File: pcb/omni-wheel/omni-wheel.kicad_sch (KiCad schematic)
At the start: 41 parts, among them IC1 AP63301WU-7, IC2 AP63301WU-7, J10 Conn_01x01_Pin, J11 Conn_01x01_Pin, J15 STLINK, J2 Motor2_output, J3 Motor4_output, J4 Motor3_output, J5 STLINK, J6 Motor1_output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

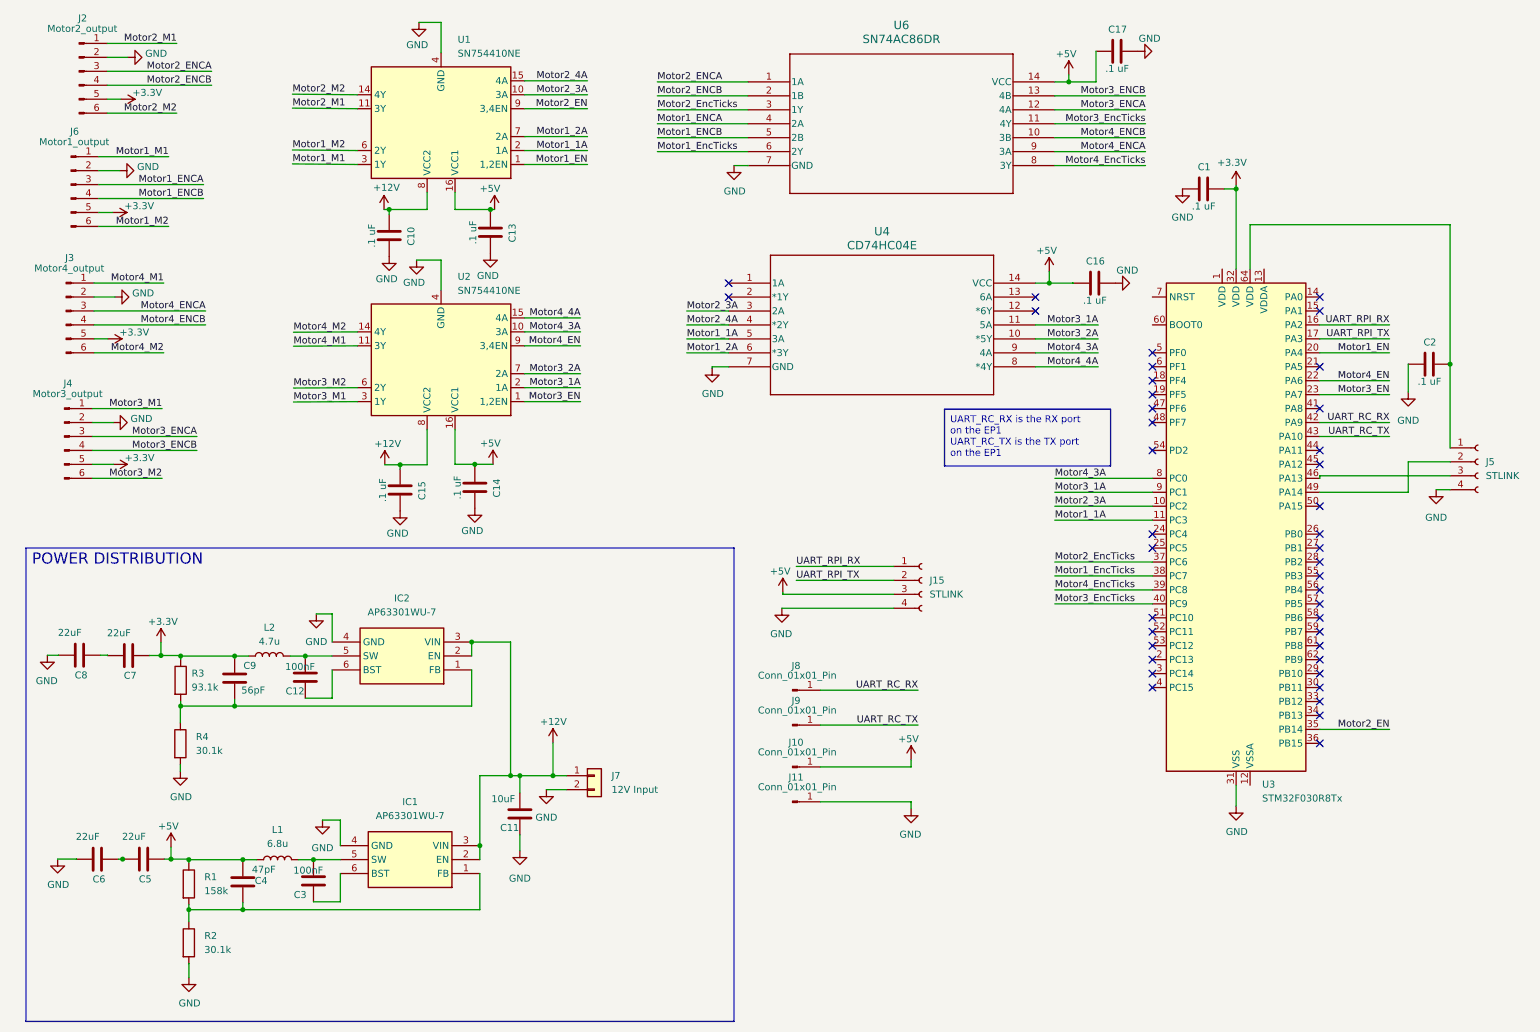
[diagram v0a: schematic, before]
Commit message: Added power test points to pcb, going to change xt size and add toggle switch next
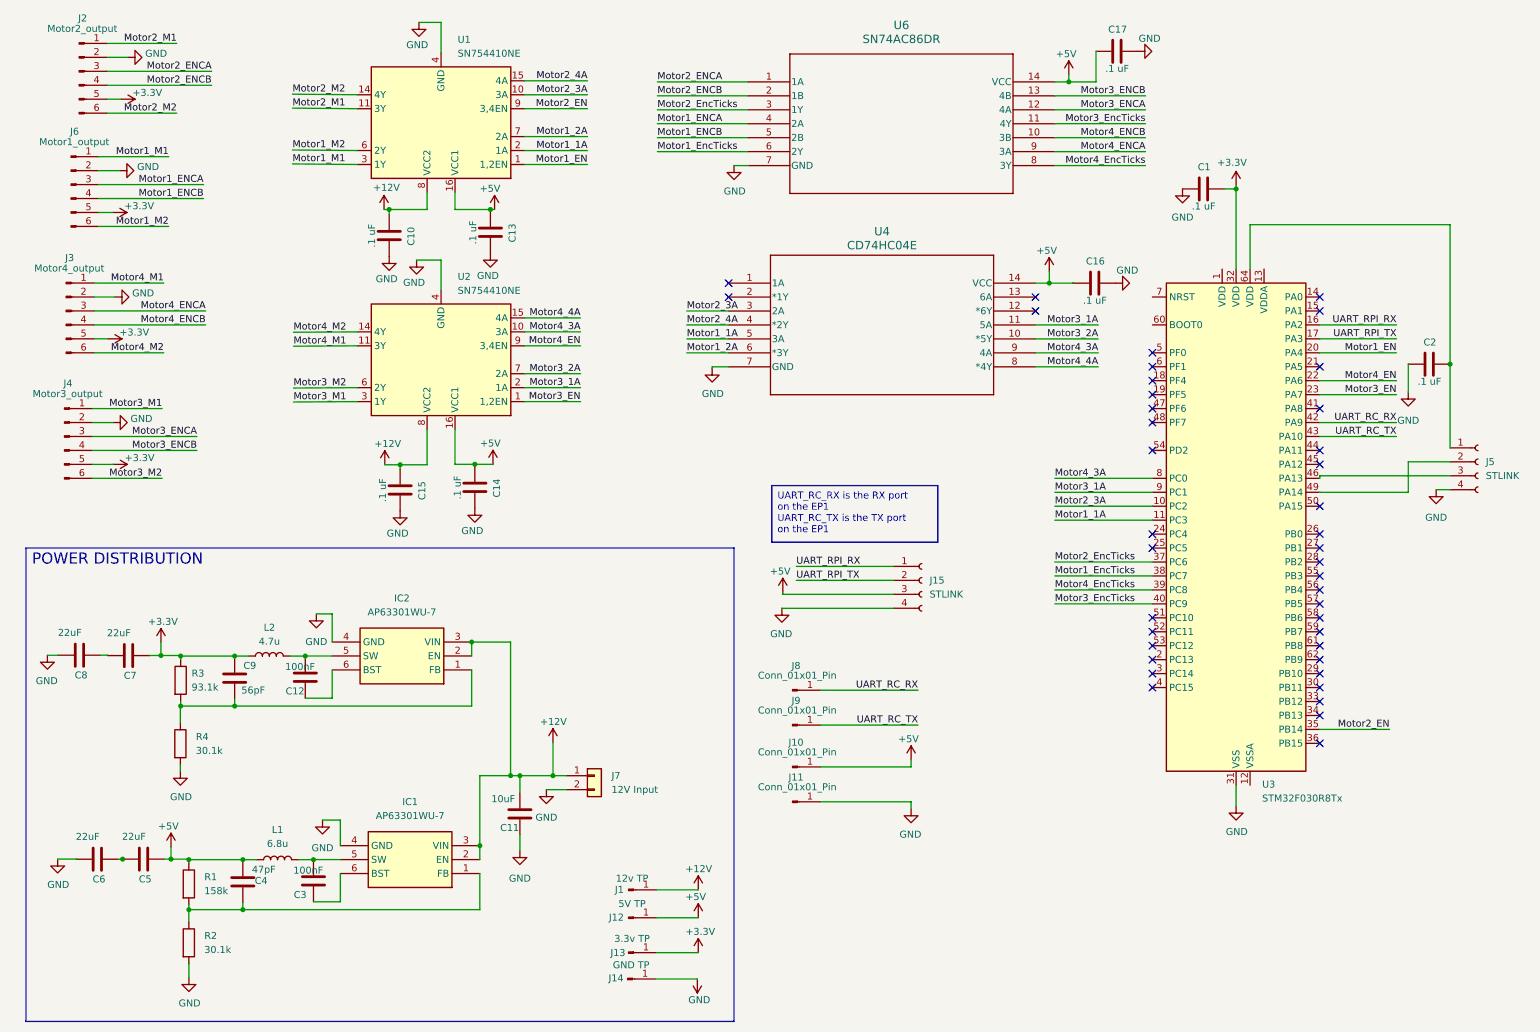
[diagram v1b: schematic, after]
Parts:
- added J1: 12v TP, TestPoint:TestPoint_THTPad_1.0x1.0mm_Drill0.5mm, symbol Connector:Conn_01x01_Pin
- added J12: 5V TP, TestPoint:TestPoint_THTPad_1.0x1.0mm_Drill0.5mm, symbol Connector:Conn_01x01_Pin
- added J13: 3.3v TP, TestPoint:TestPoint_THTPad_1.0x1.0mm_Drill0.5mm, symbol Connector:Conn_01x01_Pin
- added J14: GND TP, TestPoint:TestPoint_THTPad_1.0x1.0mm_Drill0.5mm, symbol Connector:Conn_01x01_Pin
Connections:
- net +12V: now also J1.1 (Pin_1)
- net +3.3V: now also J13.1 (Pin_1)
- net +5V: now also J12.1 (Pin_1)
- net GND: now also J14.1 (Pin_1)

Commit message: Added smaller xt connector and power switch
forgot to save schema
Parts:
- added SW1: SW_SPST, GF-123-0054:SW_GF-123-0054, symbol Switch:SW_SPST
- J7: footprint Connector_AMASS:AMASS_XT60PW-M_1x02_P7.20mm_Horizontal -> Connector_AMASS:AMASS_XT30PW-M_1x02_P2.50mm_Horizontal
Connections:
- net +12V: now also SW1.2 (B); no longer J7.1 (Pin_1)
- new net: J7.1 (Pin_1), SW1.1 (A)
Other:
- moved on the sheet: J7
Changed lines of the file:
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@@
 	)
 	(junction
-		(at 108.0081 153.2124)
-		(diameter 0)
-		(color 0 0 0 0)
-	)
-	(junction
 		(at 36.6238 131.3227)
 		(diameter 0)
@@
 	)
 	(junction
+		(at 107.9367 153.2124)
+		(diameter 0)
+		(color 0 0 0 0)
+	)
+	(junction
 		(at 40.2086 131.424)
 		(diameter 0)
@@
 	(wire
 		(pts
+			(xy 107.9367 153.0734) (xy 107.9367 153.2124)
+		)
+		(stroke
+			(width 0)
+			(type default)
+		)
+	)
+	(wire
+		(pts
 			(xy 261.62 81.28) (xy 247.65 81.28)
 		)
@@
 	(wire
 		(pts
-			(xy 106.8114 155.7524) (xy 106.8114 155.7504)
+			(xy 121.5026 155.4892) (xy 121.5026 157.4674)
 		)
 		(stroke
@@
 	(wire
 		(pts
+			(xy 109.5117 153.0734) (xy 107.9367 153.0734)
+		)
+		(stroke
+			(width 0)
+			(type default)
+		)
+	)
+	(wire
+		(pts
 			(xy 26.8028 27.4815) (xy 45.8528 27.4815)
 		)
@@
 	(wire
 		(pts
+			(xy 107.9367 153.2124) (xy 108.0081 153.2124)
+		)
+		(stroke
+			(width 0)
+			(type default)
+		)
+	)
+	(wire
+		(pts
 			(xy 78.1844 50.1004) (xy 85.09 50.1004)
 		)
@@
 	(wire
 		(pts
+			(xy 119.6717 153.0734) (xy 121.6382 153.0734)
+		)
+		(stroke
+			(width 0)
+			(type default)
+		)
+	)
+	(wire
+		(pts
 			(xy 69.2919 161.29) (xy 69.2919 165.9498)
 		)
@@
 	(wire
 		(pts
-			(xy 108.0081 153.2124) (xy 110.4721 153.2124)
-		)
-		(stroke
-			(width 0)
-			(type default)
-		)
-	)
-	(wire
-		(pts
 			(xy 54.0433 168.5038) (xy 51.5309 168.5038)
 		)
@@
 	(wire
 		(pts
-			(xy 110.4721 155.7524) (xy 106.8114 155.7524)
+			(xy 121.5026 155.4892) (xy 121.6382 155.4892)
 		)
 		(stroke
@@
 	(wire
 		(pts
+			(xy 121.6382 153.0734) (xy 121.6382 152.9492)
+		)
+		(stroke
+			(width 0)
+			(type default)
+		)
+	)
+	(wire
+		(pts
 			(xy 261.62 76.2) (xy 247.65 76.2)
 		)
@@
 	(wire
 		(pts
-			(xy 101.9818 153.2124) (xy 108.0081 153.2124)
+			(xy 101.9818 153.2124) (xy 107.9367 153.2124)
 		)
 		(stroke
@@
 	(symbol
 		(lib_id "Connector_Generic:Conn_01x02")
-		(at 115.5521 153.2124 0)
+		(at 126.7182 152.9492 0)
 		(unit 1)
 		(exclude_from_sim no)
@@
 		(fields_autoplaced yes)
 		(property "Reference" "J7"
-			(at 118.6738 153.2123 0)
+			(at 129.8399 152.9491 0)
 			(effects
 				(font
@@
 		)
 		(property "Value" "12V Input"
-			(at 118.6738 155.7523 0)
+			(at 129.8399 155.4891 0)
 			(effects
 				(font
@@
 			)
 		)
-		(property "Footprint" "Connector_AMASS:AMASS_XT60PW-M_1x02_P7.20mm_Horizontal"
-			(at 115.5521 153.2124 0)
+		(property "Footprint" "Connector_AMASS:AMASS_XT30PW-M_1x02_P2.50mm_Horizontal"
+			(at 126.7182 152.9492 0)
 			(effects
 				(font
@@
 		)
 		(property "Datasheet" "~"
-			(at 115.5521 153.2124 0)
+			(at 126.7182 152.9492 0)
 			(effects
 				(font
@@
 		)
 		(property "Description" "Generic connector, single row, 01x02, script generated (kicad-library-utils/schlib/autogen/connector/)"
-			(at 115.5521 153.2124 0)
+			(at 126.7182 152.9492 0)
 			(effects
 				(font
@@
 	)
 	(symbol
+		(lib_id "Switch:SW_SPST")
+		(at 114.5917 153.0734 180)
+		(unit 1)
+		(exclude_from_sim no)
+		(in_bom yes)
+		(on_board yes)
+		(dnp no)
+		(property "Reference" "SW1"
+			(at 114.411 150.7407 0)
+			(effects
+				(font
+					(size 1.27 1.27)
+				)
+			)
+		)
+		(property "Value" "SW_SPST"
+			(at 114.411 148.2007 0)
+			(effects
+				(font
+					(size 1.27 1.27)
+				)
+			)
+		)
+		(property "Footprint" "GF-123-0054:SW_GF-123-0054"
+			(at 114.5917 153.0734 0)
+			(effects
+				(font
+					(size 1.27 1.27)
+				)
+				(hide yes)
+			)
+		)
+		(property "Datasheet" "~"
+			(at 114.5917 153.0734 0)
+			(effects
+				(font
+					(size 1.27 1.27)
+				)
+				(hide yes)
+			)
+		)
+		(property "Description" "Single Pole Single Throw (SPST) switch"
+			(at 114.5917 153.0734 0)
+			(effects
+				(font
+					(size 1.27 1.27)
+				)
+				(hide yes)
+			)
+		)
+		(pin "2"
+		)
+		(pin "1"
+		)
+		(instances
+			(project ""
+				(path "/00bcea37-6431-4bf6-91e9-3738f9d2ffd8"
+					(reference "SW1")
+					(unit 1)
+				)
+			)
+		)
+	)
+	(symbol
 		(lib_id "power:+3.3V")
 		(at 134.3015 190.2313 180)
@@
 	(symbol
 		(lib_id "power:GND")
-		(at 106.8114 155.7504 0)
+		(at 121.5026 157.4674 0)
 		(unit 1)
 		(exclude_from_sim no)
@@
 		(fields_autoplaced yes)
 		(property "Reference" "#PWR019"
-			(at 106.8114 162.1004 0)
+			(at 121.5026 163.8174 0)
 			(effects
 				(font
@@
 		)
 		(property "Value" "GND"
-			(at 106.8114 160.8157 0)
+			(at 121.5026 162.5327 0)
 			(effects
 				(font
@@
 		)
 		(property "Footprint" ""
-			(at 106.8114 155.7504 0)
+			(at 121.5026 157.4674 0)
 			(effects
 				(font
@@
 		)
 		(property "Datasheet" ""
-			(at 106.8114 155.7504 0)
+			(at 121.5026 157.4674 0)
 			(effects
 				(font
@@
 		)
 		(property "Description" "Power symbol creates a global label with name \"GND\" , ground"
-			(at 106.8114 155.7504 0)
+			(at 121.5026 157.4674 0)
 			(effects
 				(font

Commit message: purchased this iteration of the board
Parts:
- SW1: digikey# (none) -> CWI333-ND; manf# (none) -> GF-123-0054
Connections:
- net GND: now also J7.1 (Pin_1); no longer J7.2 (Pin_2)
- net at SW1.1 (A): now also J7.2 (Pin_2); no longer J7.1 (Pin_1)
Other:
- moved on the sheet: J7
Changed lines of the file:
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@@
 	(wire
 		(pts
-			(xy 121.5026 155.4892) (xy 121.5026 157.4674)
-		)
-		(stroke
-			(width 0)
-			(type default)
-		)
-	)
-	(wire
-		(pts
 			(xy 93.2024 128.87) (xy 100.2871 128.87)
 		)
@@
 	(wire
 		(pts
+			(xy 124.3955 144.8826) (xy 121.6091 144.8826)
+		)
+		(stroke
+			(width 0)
+			(type default)
+		)
+	)
+	(wire
+		(pts
 			(xy 198.3856 63.5124) (xy 202.6638 63.5124)
 		)
@@
 	(wire
 		(pts
+			(xy 119.6717 153.0923) (xy 119.6717 153.0734)
+		)
+		(stroke
+			(width 0)
+			(type default)
+		)
+	)
+	(wire
+		(pts
 			(xy 207.3005 76.2124) (xy 195.8705 76.2124)
 		)
@@
 	(wire
 		(pts
+			(xy 124.3955 150.5523) (xy 124.3955 144.8826)
+		)
+		(stroke
+			(width 0)
+			(type default)
+		)
+	)
+	(wire
+		(pts
 			(xy 134.3015 190.2313) (xy 126.6815 190.2313)
 		)
@@
 	(wire
 		(pts
-			(xy 119.6717 153.0734) (xy 121.6382 153.0734)
-		)
-		(stroke
-			(width 0)
-			(type default)
-		)
-	)
-	(wire
-		(pts
 			(xy 69.2919 161.29) (xy 69.2919 165.9498)
 		)
@@
 	(wire
 		(pts
-			(xy 121.5026 155.4892) (xy 121.6382 155.4892)
-		)
-		(stroke
-			(width 0)
-			(type default)
-		)
-	)
-	(wire
-		(pts
 			(xy 113.03 74.93) (xy 102.87 74.93)
 		)
@@
 	(wire
 		(pts
-			(xy 121.6382 153.0734) (xy 121.6382 152.9492)
-		)
-		(stroke
-			(width 0)
-			(type default)
-		)
-	)
-	(wire
-		(pts
 			(xy 261.62 76.2) (xy 247.65 76.2)
 		)
@@
 	(wire
 		(pts
+			(xy 124.3955 153.0923) (xy 119.6717 153.0923)
+		)
+		(stroke
+			(width 0)
+			(type default)
+		)
+	)
+	(wire
+		(pts
 			(xy 40.1561 140.5536) (xy 40.1561 143.5757)
 		)
@@
 	(symbol
 		(lib_id "Connector_Generic:Conn_01x02")
-		(at 126.7182 152.9492 0)
+		(at 129.4755 150.5523 0)
 		(unit 1)
 		(exclude_from_sim no)
@@
 		(fields_autoplaced yes)
 		(property "Reference" "J7"
-			(at 129.8399 152.9491 0)
+			(at 132.5972 150.5522 0)
 			(effects
 				(font
@@
 		)
 		(property "Value" "12V Input"
-			(at 129.8399 155.4891 0)
+			(at 132.5972 153.0922 0)
 			(effects
 				(font
@@
 		)
 		(property "Footprint" "Connector_AMASS:AMASS_XT30PW-M_1x02_P2.50mm_Horizontal"
-			(at 126.7182 152.9492 0)
+			(at 129.4755 150.5523 0)
 			(effects
 				(font
@@
 		)
 		(property "Datasheet" "~"
-			(at 126.7182 152.9492 0)
+			(at 129.4755 150.5523 0)
 			(effects
 				(font
@@
 		)
 		(property "Description" "Generic connector, single row, 01x02, script generated (kicad-library-utils/schlib/autogen/connector/)"
-			(at 126.7182 152.9492 0)
+			(at 129.4755 150.5523 0)
 			(effects
 				(font
@@
 			)
 		)
+		(property "digikey#" "CWI333-ND"
+			(at 114.5917 153.0734 0)
+			(effects
+				(font
+					(size 1.27 1.27)
+				)
+				(hide yes)
+			)
+		)
+		(property "manf#" "GF-123-0054"
+			(at 114.5917 153.0734 0)
+			(effects
+				(font
+					(size 1.27 1.27)
+				)
+				(hide yes)
+			)
+		)
 		(pin "2"
 		)
@@
 	(symbol
 		(lib_id "power:GND")
-		(at 121.5026 157.4674 0)
+		(at 121.6091 144.8826 0)
 		(unit 1)
 		(exclude_from_sim no)
@@
 		(fields_autoplaced yes)
 		(property "Reference" "#PWR019"
-			(at 121.5026 163.8174 0)
+			(at 121.6091 151.2326 0)
 			(effects
 				(font
@@
 		)
 		(property "Value" "GND"
-			(at 121.5026 162.5327 0)
+			(at 121.6091 149.9479 0)
 			(effects
 				(font
@@
 		)
 		(property "Footprint" ""
-			(at 121.5026 157.4674 0)
+			(at 121.6091 144.8826 0)
 			(effects
 				(font
@@
 		)
 		(property "Datasheet" ""
-			(at 121.5026 157.4674 0)
+			(at 121.6091 144.8826 0)
 			(effects
 				(font
@@
 		)
 		(property "Description" "Power symbol creates a global label with name \"GND\" , ground"
-			(at 121.5026 157.4674 0)
+			(at 121.6091 144.8826 0)
 			(effects
 				(font
